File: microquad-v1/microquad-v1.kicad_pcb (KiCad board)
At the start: 2 copper layers, 83.8 x 74.3 mm, 79 parts, among them J1 USB_microB_2040002-1, M1 Motor_DC, M2 Motor_DC, M3 Motor_DC, M4 Motor_DC, M5 Motor_DC, M6 Motor_DC, Q1 Q_NMOS_GSD, Q2 Q_NMOS_GSD, Q3 Q_NMOS_GSD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

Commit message: Rerouted vbat and moved USB
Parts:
- moved J1 3.11 mm to (226.0, 83.6)
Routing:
- net /VBAT: track 192.4 -> 232.1 mm
- net Net-(J1-Pad3): track 2.64 -> 5.95 mm
- net Net-(J1-Pad2): track 10.9 -> 14.2 mm
- net GND: track 286.2 -> 289.5 mm
- net /USB interface/5V: track 30.1 -> 33.1 mm

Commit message: Ready to submit
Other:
- board text added: "Eric Marie-Caroline"
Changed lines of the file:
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@@
   (general
     (links 185)
-    (no_connects 5)
-    (area 177.8 25.4 304.800001 152.400001)
+    (no_connects 0)
+    (area 199.314999 55.489136 283.285001 129.930864)
     (thickness 1.6)
-    (drawings 99)
+    (drawings 101)
     (tracks 801)
     (zones 0)
@@
   (page A4)
   (layers
-    (0 F.Cu signal)
-    (31 B.Cu signal)
-    (32 B.Adhes user)
-    (33 F.Adhes user)
-    (34 B.Paste user)
+    (0 F.Cu signal hide)
+    (31 B.Cu signal hide)
+    (32 B.Adhes user hide)
+    (33 F.Adhes user hide)
+    (34 B.Paste user hide)
     (35 F.Paste user hide)
     (36 B.SilkS user)
-    (37 F.SilkS user)
-    (38 B.Mask user)
-    (39 F.Mask user)
-    (40 Dwgs.User user)
-    (41 Cmts.User user)
+    (37 F.SilkS user hide)
+    (38 B.Mask user hide)
+    (39 F.Mask user hide)
+    (40 Dwgs.User user hide)
+    (41 Cmts.User user hide)
     (42 Eco1.User user)
     (43 Eco2.User user)
@@
   )
   (setup
-    (last_trace_width 0.4)
+    (last_trace_width 0.25)
     (user_trace_width 0.2)
     (user_trace_width 0.25)
@@
     (pad_to_mask_clearance 0.2)
     (aux_axis_origin 0 0)
-    (visible_elements 7FFFFFFF)
+    (visible_elements 7FFFBFFF)
     (pcbplotparams
       (layerselection 0x00030_80000001)
@@
     )
   )
+  (gr_text "Eric\nMarie-Caroline" (at 241.3 109.22) (layer B.SilkS)
+    (effects (font (size 2 1.5) (thickness 0.3)) (justify mirror))
+  )
+  (gr_line (start 276.86 99.06) (end 273.685 99.06) (layer Edge.Cuts) (width 0.15))
   (gr_text BT (at 232.3465 105.4735 30) (layer B.SilkS)
     (effects (font (size 1.5 1.5) (thickness 0.3)) (justify mirror))
@@
   (segment (start 252.4357 89.76) (end 252.0257 90.17) (width 0.2) (layer F.Cu) (net 6))
   (segment (start 253 89.76) (end 252.4357 89.76) (width 0.2) (layer F.Cu) (net 6) (status 10))
+  (segment (start 214.9 96.52) (end 214.9 96.645) (width 0.4) (layer F.Cu) (net 7))
+  (segment (start 219.201248 96.266) (end 221.869 96.266) (width 0.4) (layer F.Cu) (net 7))
+  (segment (start 214.9 96.645) (end 215.831473 97.576473) (width 0.4) (layer F.Cu) (net 7))
+  (segment (start 215.831473 97.576473) (end 217.890775 97.576473) (width 0.4) (layer F.Cu) (net 7))
+  (segment (start 217.890775 97.576473) (end 219.201248 96.266) (width 0.4) (layer F.Cu) (net 7))
   (segment (start 254.940284 78.235665) (end 251.164335 78.235665) (width 0.4) (layer F.Cu) (net 7))
   (segment (start 251.164335 78.235665) (end 250.19 79.21) (width 0.4) (layer F.Cu) (net 7))
@@
   (segment (start 221.615 96.52) (end 221.869 96.266) (width 0.4) (layer F.Cu) (net 7))
   (segment (start 221.869 96.266) (end 224.79 93.345) (width 0.4) (layer F.Cu) (net 7))
-  (segment (start 217.6055 97.545) (end 218.8845 96.266) (width 0.4) (layer F.Cu) (net 7))
-  (segment (start 218.8845 96.266) (end 221.869 96.266) (width 0.4) (layer F.Cu) (net 7))
-  (segment (start 214.9 96.645) (end 215.8 97.545) (width 0.4) (layer F.Cu) (net 7))
-  (segment (start 215.8 97.545) (end 217.6055 97.545) (width 0.4) (layer F.Cu) (net 7))
   (segment (start 228.157943 77.56729) (end 228.981 77.787827) (width 0.4) (layer F.Cu) (net 7))
   (segment (start 226.342482 75.6285) (end 226.821673 75.6285) (width 0.4) (layer F.Cu) (net 7))
@@
   (segment (start 247.842943 73.75729) (end 249.005074 78.094421) (width 0.4) (layer F.Cu) (net 7))
   (segment (start 249.005074 78.094421) (end 248.359495 78.74) (width 0.4) (layer F.Cu) (net 7))
-  (segment (start 214.9 96.52) (end 214.9 96.645) (width 0.4) (layer F.Cu) (net 7) (status 30))
   (segment (start 212.09 94.11) (end 212.09 96.52) (width 0.4) (layer F.Cu) (net 7) (status 30))
   (segment (start 212.09 96.52) (end 214.9 96.52) (width 0.4) (layer F.Cu) (net 7) (status 30))

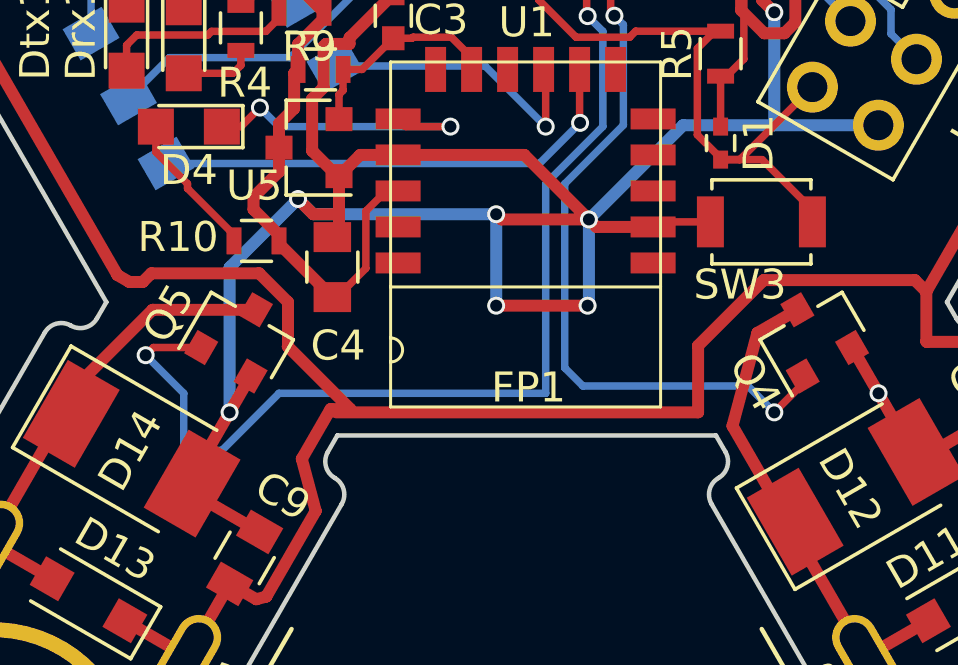
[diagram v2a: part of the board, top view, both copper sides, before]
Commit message: Removed copper pour from underneath bluetooth module
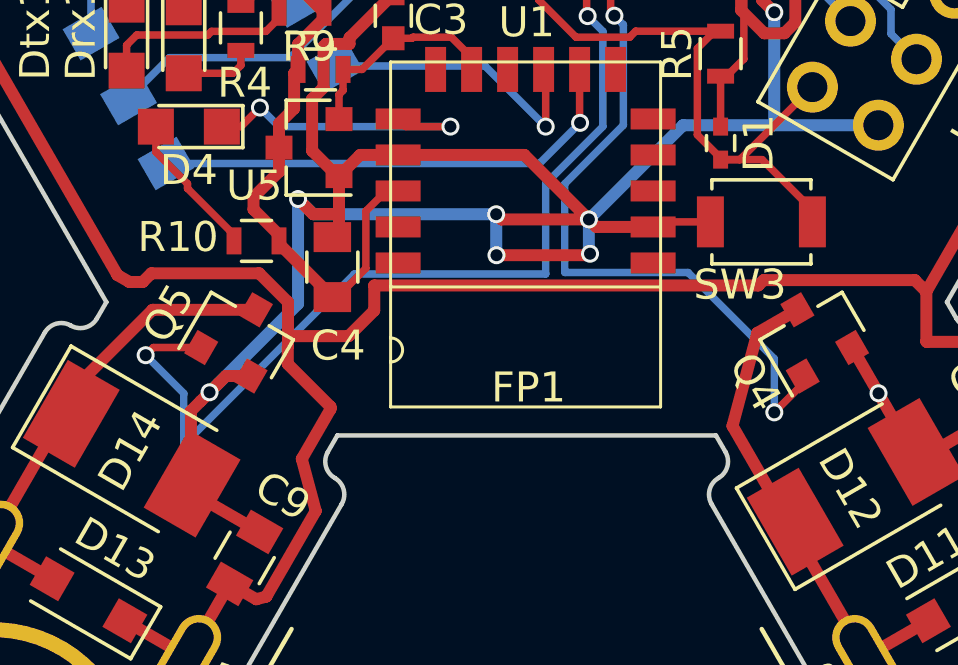
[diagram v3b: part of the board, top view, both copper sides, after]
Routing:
- net GND: track 289.5 -> 286.6 mm
- net /Motor5/ENABLE: track 33.7 -> 31.1 mm
- net /VBAT: track 232.1 -> 230.9 mm
- net /Motor4/ENABLE: track 23.5 -> 22.7 mm
